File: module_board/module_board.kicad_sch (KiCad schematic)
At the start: 1 part, among them J1 Bus_M.2_Socket_B

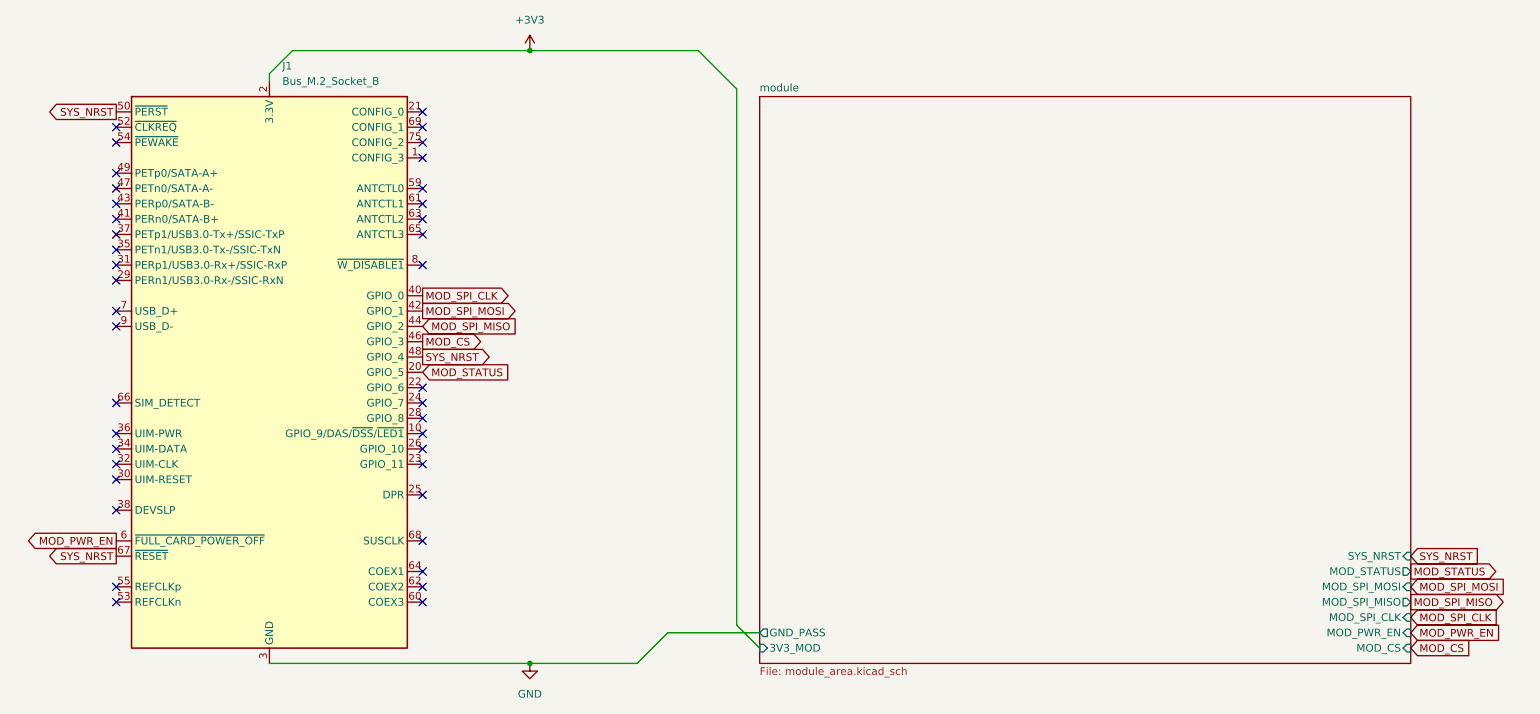
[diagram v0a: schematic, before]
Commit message: feat: finish all essential schematics (i think?)
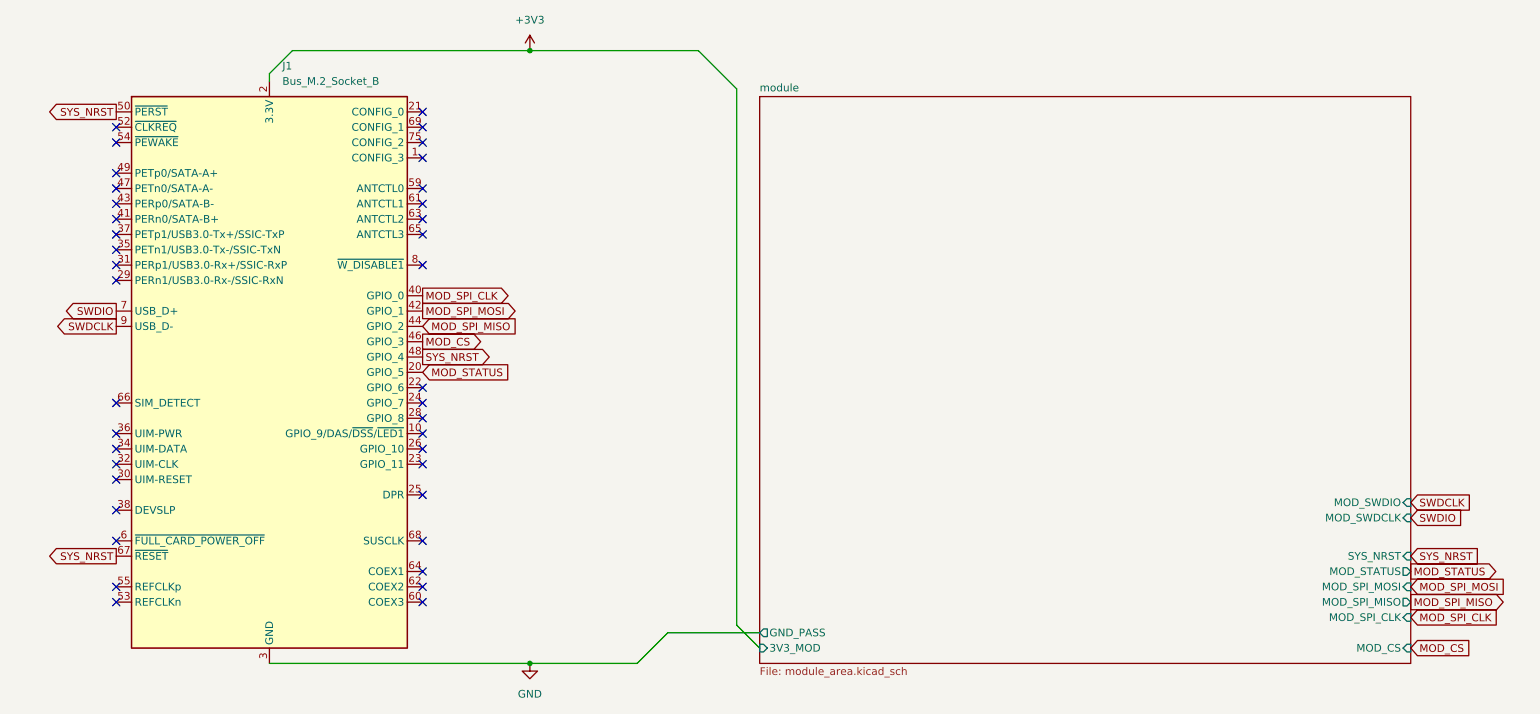
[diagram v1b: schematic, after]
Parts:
- J1: now left out of the parts list
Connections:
- net SWDIO: now reaches J1.7 (USB_D+)
- net SWDCLK: now reaches J1.9 (USB_D-)
- net MOD_PWR_EN: no longer names the net of J1.6 (~{FULL_CARD_POWER_OFF})
- no-connect marks 40 -> 39
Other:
- sheet module ports: added MOD_SWDCLK, MOD_SWDIO; removed MOD_PWR_EN
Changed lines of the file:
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@@
-	)
-	(no_connect
-		(at 27.94 87.63)
 	)
 	(no_connect
@@
 	)
 	(no_connect
+		(at 27.94 125.73)
+	)
+	(no_connect
 		(at 27.94 133.35)
 	)
@@
 	)
 	(no_connect
-		(at 27.94 90.17)
-	)
-	(no_connect
 		(at 78.74 113.03)
 	)
@@
 			(width 0)
 			(type default)
+		)
+	)
+	(global_label "SWDIO"
+		(shape output)
+		(at 27.94 87.63 180)
+		(fields_autoplaced yes)
+		(effects
+			(font
+				(size 1.27 1.27)
+			)
+			(justify right)
+		)
+		(property "Intersheetrefs" "${INTERSHEET_REFS}"
+			(at 19.0886 87.63 0)
+			(effects
+				(font
+					(size 1.27 1.27)
+				)
+				(justify right)
+				(hide yes)
+			)
+		)
+	)
+	(global_label "SWDIO"
+		(shape input)
+		(at 242.57 121.92 0)
+		(fields_autoplaced yes)
+		(effects
+			(font
+				(size 1.27 1.27)
+			)
+			(justify left)
+		)
+		(property "Intersheetrefs" "${INTERSHEET_REFS}"
+			(at 251.4214 121.92 0)
+			(effects
+				(font
+					(size 1.27 1.27)
+				)
+				(justify left)
+				(hide yes)
+			)
 		)
 	)
@@
 		)
 	)
-	(global_label "MOD_PWR_EN"
-		(shape output)
-		(at 27.94 125.73 180)
-		(fields_autoplaced yes)
-		(effects
-			(font
-				(size 1.27 1.27)
-			)
-			(justify right)
-		)
-		(property "Intersheetrefs" "${INTERSHEET_REFS}"
-			(at 12.4968 125.73 0)
-			(effects
-				(font
-					(size 1.27 1.27)
-				)
-				(justify right)
-				(hide yes)
-			)
-		)
-	)
 	(global_label "SYS_NRST"
 		(shape input)
@@
 		)
 	)
+	(global_label "SWDCLK"
+		(shape output)
+		(at 27.94 90.17 180)
+		(fields_autoplaced yes)
+		(effects
+			(font
+				(size 1.27 1.27)
+			)
+			(justify right)
+		)
+		(property "Intersheetrefs" "${INTERSHEET_REFS}"
+			(at 17.4558 90.17 0)
+			(effects
+				(font
+					(size 1.27 1.27)
+				)
+				(justify right)
+				(hide yes)
+			)
+		)
+	)
 	(global_label "SYS_NRST"
 		(shape output)
@@
 		)
 	)
-	(global_label "MOD_PWR_EN"
-		(shape input)
-		(at 242.57 140.97 0)
-		(fields_autoplaced yes)
-		(effects
-			(font
-				(size 1.27 1.27)
-			)
-			(justify left)
-		)
-		(property "Intersheetrefs" "${INTERSHEET_REFS}"
-			(at 258.0132 140.97 0)
-			(effects
-				(font
-					(size 1.27 1.27)
-				)
-				(justify left)
-				(hide yes)
-			)
-		)
-	)
 	(global_label "MOD_SPI_MOSI"
 		(shape output)
@@
 		(property "Intersheetrefs" "${INTERSHEET_REFS}"
 			(at 95.3928 87.63 0)
+			(effects
+				(font
+					(size 1.27 1.27)
+				)
+				(justify left)
+				(hide yes)
+			)
+		)
+	)
+	(global_label "SWDCLK"
+		(shape input)
+		(at 242.57 119.38 0)
+		(fields_autoplaced yes)
+		(effects
+			(font
+				(size 1.27 1.27)
+			)
+			(justify left)
+		)
+		(property "Intersheetrefs" "${INTERSHEET_REFS}"
+			(at 253.0542 119.38 0)
 			(effects
 				(font
@@
 		(unit 1)
 		(exclude_from_sim no)
-		(in_bom yes)
-		(on_board yes)
+		(in_bom no)
+		(on_board no)
 		(dnp no)
 		(fields_autoplaced yes)
@@
 			)
 		)
-		(pin "MOD_PWR_EN" input
-			(at 242.57 140.97 0)
-			(effects
-				(font
-					(size 1.27 1.27)
-				)
-				(justify right)
-			)
-		)
 		(pin "MOD_SPI_CLK" input
 			(at 242.57 138.43 0)
@@
 			(effects
 				(font
+					(size 1.27 1.27)
+				)
+				(justify right)
+			)
+		)
+		(pin "MOD_SWDCLK" input
+			(at 242.57 121.92 0)
+			(effects
+				(font
+					(size 1.27 1.27)
+				)
+				(justify right)
+			)
+		)
+		(pin "MOD_SWDIO" input
+			(at 242.57 119.38 0)
+			(effects
+				(font
